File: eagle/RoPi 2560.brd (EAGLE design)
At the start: 85.1 x 56.1 mm, 50 parts, among them J1 AVR_SPI_PRG_6PTH, U1 ATMEGA2560AU, U2 MAX3378EEUD, U3 L298_BRIDGE_DRIVER, U4 L298_BRIDGE_DRIVER, Y1 16M

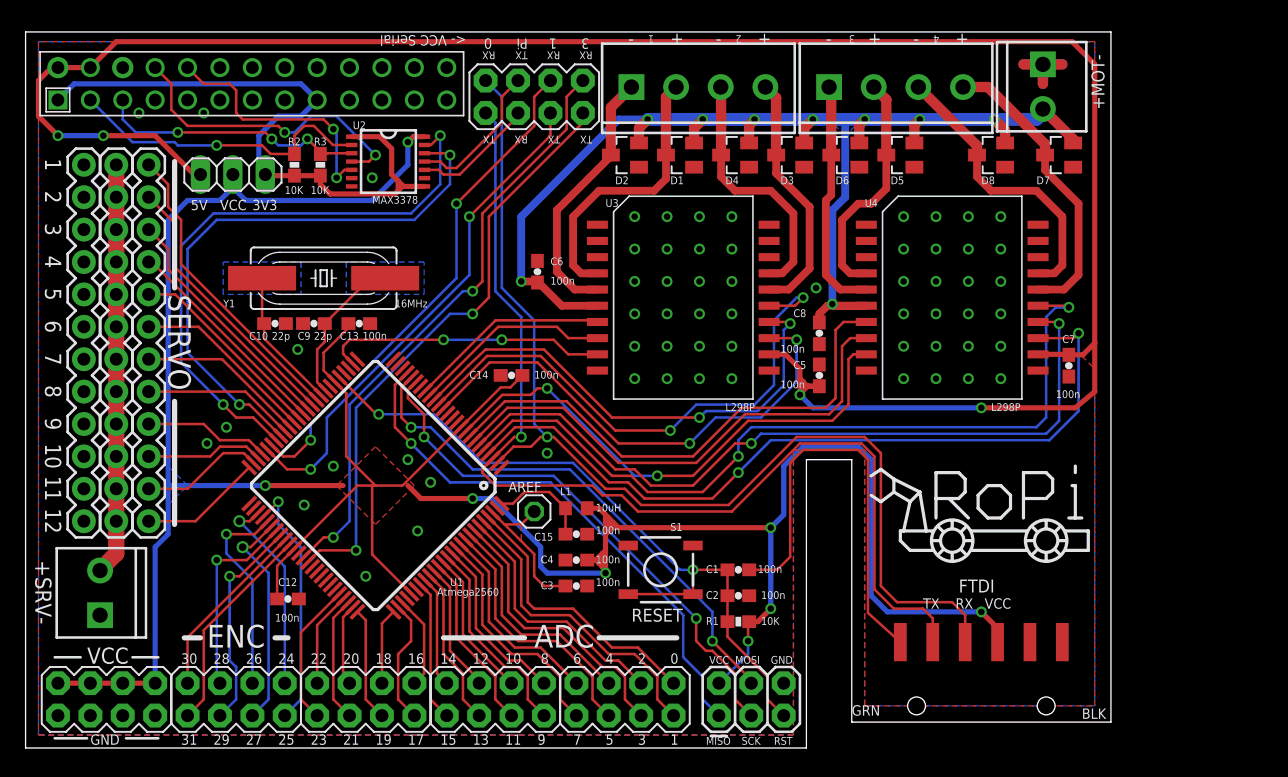
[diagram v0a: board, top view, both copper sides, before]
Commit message: Removed 5V <-> 3V3 selector jumper as an ATmega2560 running at 16MHz can only be supplied 5V
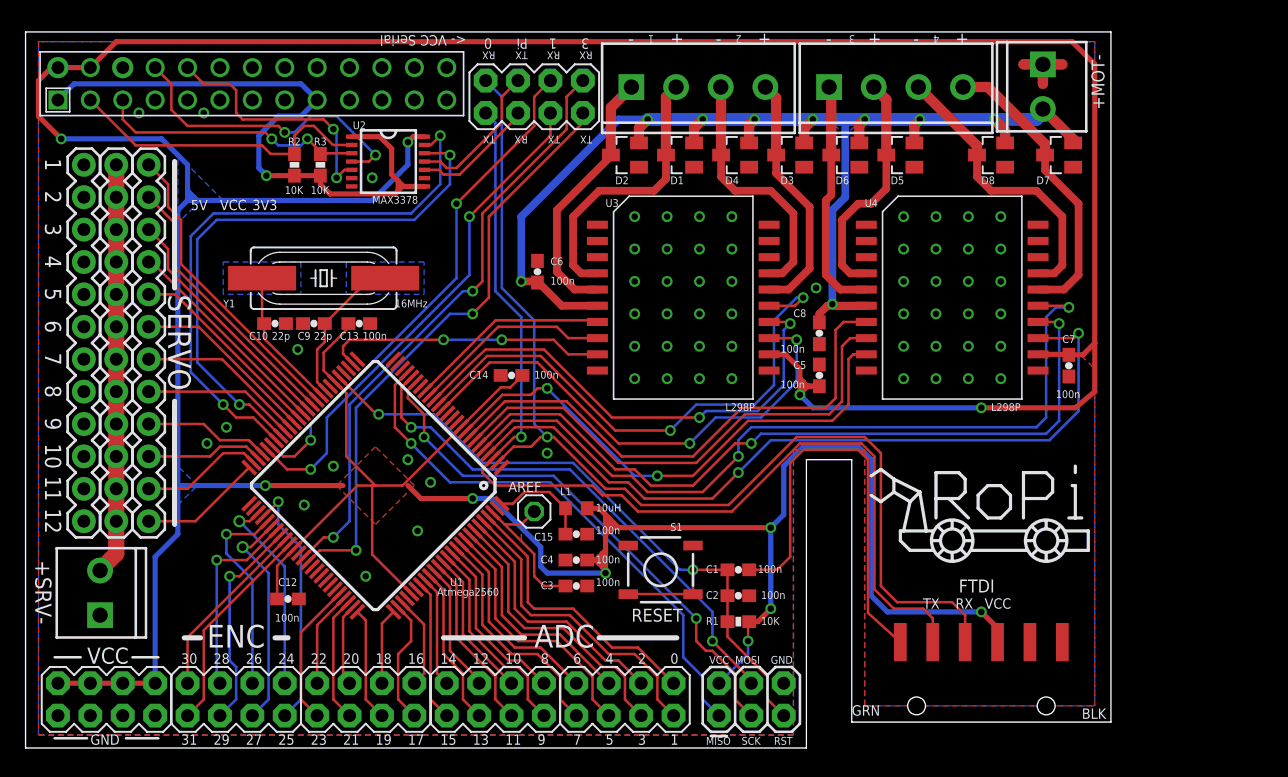
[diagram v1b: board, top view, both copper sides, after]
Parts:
- removed JP6: (no value), pinhead:1X03
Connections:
- removed net VCC: C12.1, C13.1, C14.1, C4.1, J1.2, JP1.4, JP6.2, L1.2, R1.2, U$2.1, U$2.3, U$2.5, U$2.7, U1.10, U1.31, U1.61, U1.80, U2.14
- net 3.3V: no longer JP6.1
- net 5V: now also C12.1, C13.1, C14.1, C4.1, J1.2, JP1.4, L1.2, R1.2, U$2.1, U$2.3, U$2.5, U$2.7, U1.10, U1.31, U1.61, U1.80, U2.14; no longer JP6.3
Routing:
- net 5V: track 166.6 -> 399.8 mm, vias 4 -> 11
- net VCC: track 233.1 -> 0.00 mm, vias 8 -> 0
- net AVR_SDA: track 46.8 -> 46.2 mm
- net AVR_SCL: track 45.2 -> 44.5 mm
- net PI_SDA: vias 1 -> 0
- net PI_SCL: vias 3 -> 2
- net 3.3V: vias 0 -> 1
- added copper zone on layer 16, net 5V
- removed copper zone on layer 1, net VCC
- removed copper zone on layer 16, net VCC

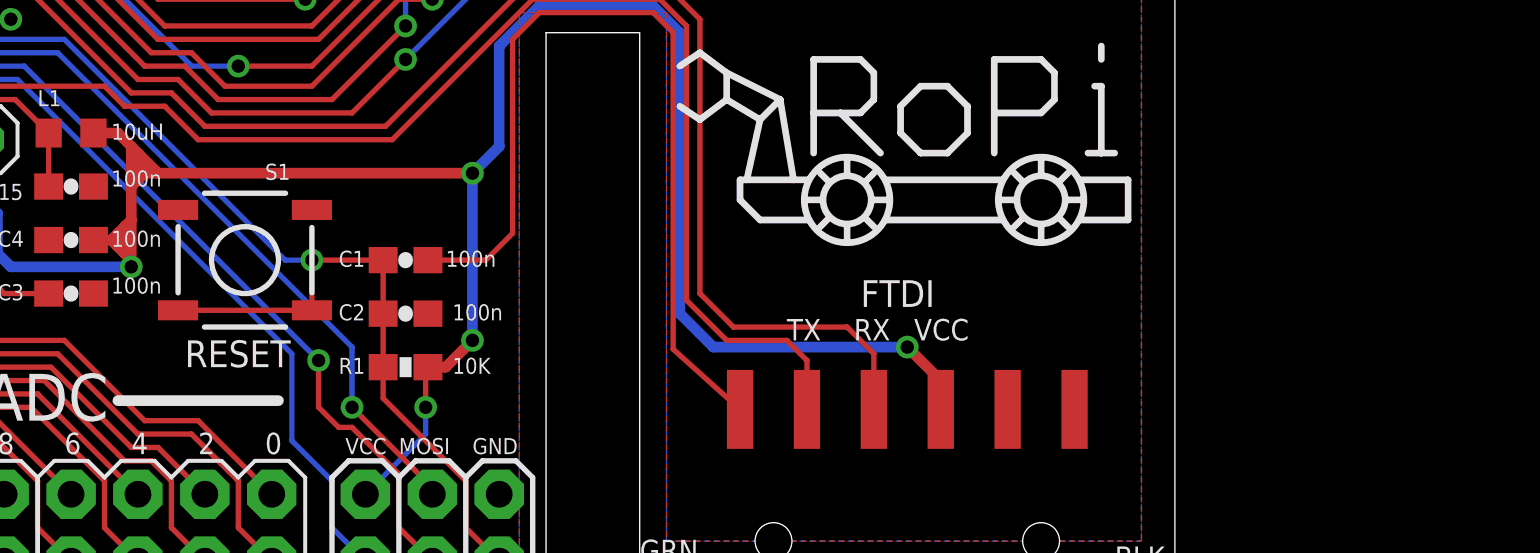
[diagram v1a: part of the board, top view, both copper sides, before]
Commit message: Leaving 2nd revision board as-is; will not be ordering 0.2 board.
0.3 is a complete re-routing and layout adjustment. The ATmega has been
moved closer to the bottom left corner. The slot for the camera cable has
been adjusted to the left a bit to better sit squarely over the connector.

The reset switch and passives have been moved over the ethernet connector
adjacent to the FTDI header. The ISP header has also been moved away from
the edge to allow a normal IDC connector to fit.

Pullups have been added to the 5V side of the I2C bus.

The motor controller region has been spread out slightly for easier soldering.

Still need to finish routing the level shifter for the Pi's I2C and UART,
all of the ATmega's UARTS, ISP, motor control signals, and power.
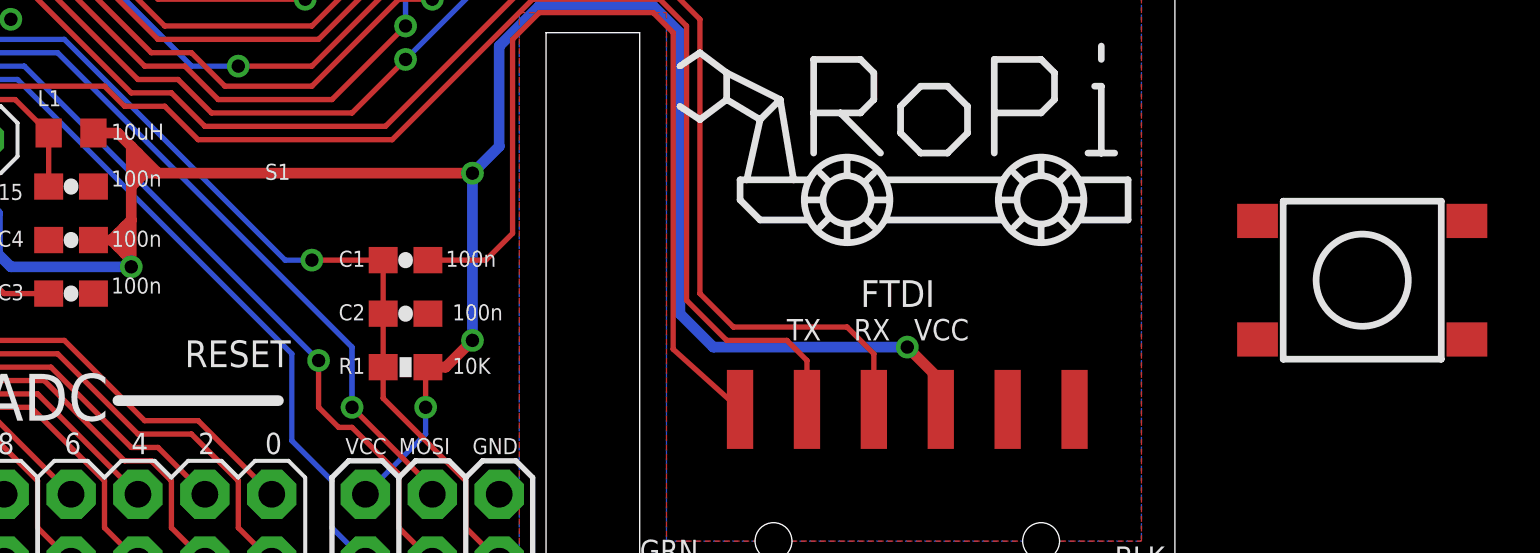
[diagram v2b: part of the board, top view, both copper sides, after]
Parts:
- S1: value (none) -> SWITCH-MOMENTARY-2SMD-4; device SparkFun-Electromechanical:TACTILE_SWITCH_SMD -> SparkFun-Electromechanical:TACTILE_SWITCH_TALL
- moved S1 42.4 mm to (92.2, 13.2), turned to 180 degrees
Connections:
- net GND: now also S1.A2; no longer S1.1, S1.2
- net RST: now also S1.B2; no longer S1.3, S1.4
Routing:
- net RST: track 56.9 -> 49.9 mm
